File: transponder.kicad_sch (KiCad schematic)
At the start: 5 parts, among them J1 Antenna SMA, J2 DB15_Female, J3 Screw_Terminal_01x08, J4 Screw_Terminal_01x12

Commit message: Proof reading and snagging updates
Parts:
- TB6: renamed from J4; symbol Connector:Screw_Terminal_01x12 -> Connector:Screw_Terminal_01x10
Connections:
- net GND: no longer TB6.11 (Pin_11), TB6.12 (Pin_12)
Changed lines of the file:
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@@
   (title_block
     (title "Europa Transponder")
-    (date "2022-11-24")
-    (rev "4")
-    (comment 1 "Comment 1")
+    (date "2022-12-22")
+    (rev "5")
   )
   (junction (at 180.34 63.5) (diameter 0) (color 0 0 0 0)
-  )
-  (junction (at 180.34 83.82) (diameter 0) (color 0 0 0 0)
   )
   (junction (at 180.34 60.96) (diameter 0) (color 0 0 0 0)
@@
   (junction (at 180.34 78.74) (diameter 0) (color 0 0 0 0)
   )
-  (junction (at 180.34 58.42) (diameter 0) (color 0 0 0 0)
-  )
   (junction (at 180.34 81.28) (diameter 0) (color 0 0 0 0)
   )
-  (junction (at 120.65 58.42) (diameter 0) (color 0 0 0 0)
+  (junction (at 120.65 60.96) (diameter 0) (color 0 0 0 0)
   )
   (junction (at 180.34 76.2) (diameter 0) (color 0 0 0 0)
@@
     (stroke (width 0) (type default) (color 0 0 0 0))
   )
-  (wire (pts (xy 180.34 83.82) (xy 180.34 87.63))
+  (wire (pts (xy 180.34 81.28) (xy 180.34 87.63))
     (stroke (width 0) (type default) (color 0 0 0 0))
   )
   (wire (pts (xy 180.34 78.74) (xy 180.34 81.28))
-    (stroke (width 0) (type default) (color 0 0 0 0))
-  )
-  (wire (pts (xy 180.34 81.28) (xy 180.34 83.82))
     (stroke (width 0) (type default) (color 0 0 0 0))
   )
@@
     (stroke (width 0) (type default) (color 0 0 0 0))
   )
-  (wire (pts (xy 180.34 55.88) (xy 180.34 58.42))
-    (stroke (width 0) (type default) (color 0 0 0 0))
-  )
   (polyline (pts (xy 109.22 44.45) (xy 109.22 123.19))
     (stroke (width 0) (type default) (color 0 0 0 0))
@@
   )
   (wire (pts (xy 171.45 91.44) (xy 171.45 105.41))
+    (stroke (width 0) (type default) (color 0 0 0 0))
+  )
+  (wire (pts (xy 120.65 60.96) (xy 180.34 60.96))
     (stroke (width 0) (type default) (color 0 0 0 0))
   )
@@
   )
   (wire (pts (xy 171.45 105.41) (xy 177.8 105.41))
-    (stroke (width 0) (type default) (color 0 0 0 0))
-  )
-  (wire (pts (xy 120.65 58.42) (xy 180.34 58.42))
     (stroke (width 0) (type default) (color 0 0 0 0))
   )
@@
     (effects (font (size 1.27 1.27)) (justify left bottom))
   )
-  (symbol (lib_id "Connector:Screw_Terminal_01x12") (at 185.42 68.58 0) (unit 1)
+  (symbol (lib_id "Connector:Screw_Terminal_01x10") (at 185.42 68.58 0) (unit 1)
     (in_bom yes) (on_board yes) (fields_autoplaced)
-    (property "Reference" "J4" (id 0) (at 187.96 68.5799 0)
+    (property "Reference" "TB6" (id 0) (at 187.96 68.5799 0)
       (effects (font (size 1.27 1.27)) (justify left))
     )
@@
     (pin "1")
     (pin "10")
-    (pin "11")
-    (pin "12")
     (pin "2")
     (pin "3")

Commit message: Added Tag Blocks
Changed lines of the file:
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@@
   (junction (at 180.34 63.5) (diameter 0) (color 0 0 0 0)
+  )
+  (junction (at 165.1 60.96) (diameter 0) (color 0 0 0 0)
   )
   (junction (at 180.34 60.96) (diameter 0) (color 0 0 0 0)
@@
   (junction (at 180.34 66.04) (diameter 0) (color 0 0 0 0)
   )
+  (junction (at 166.37 91.44) (diameter 0) (color 0 0 0 0)
+  )
   (polyline (pts (xy 85.09 44.45) (xy 85.09 123.19))
     (stroke (width 0) (type default) (color 0 0 0 0))
@@
   )
   (wire (pts (xy 180.34 78.74) (xy 180.34 81.28))
+    (stroke (width 0) (type default) (color 0 0 0 0))
+  )
+  (wire (pts (xy 165.1 60.96) (xy 180.34 60.96))
+    (stroke (width 0) (type default) (color 0 0 0 0))
+  )
+  (wire (pts (xy 166.37 91.44) (xy 171.45 91.44))
     (stroke (width 0) (type default) (color 0 0 0 0))
   )
@@
     (stroke (width 0) (type default) (color 0 0 0 0))
   )
+  (wire (pts (xy 165.1 58.42) (xy 165.1 60.96))
+    (stroke (width 0) (type default) (color 0 0 0 0))
+  )
   (wire (pts (xy 171.45 91.44) (xy 171.45 105.41))
     (stroke (width 0) (type default) (color 0 0 0 0))
   )
-  (wire (pts (xy 120.65 60.96) (xy 180.34 60.96))
+  (wire (pts (xy 120.65 60.96) (xy 165.1 60.96))
     (stroke (width 0) (type default) (color 0 0 0 0))
   )
@@
     (stroke (width 0) (type default) (color 0 0 0 0))
   )
+  (wire (pts (xy 166.37 87.63) (xy 166.37 91.44))
+    (stroke (width 0) (type default) (color 0 0 0 0))
+  )
   (polyline (pts (xy 219.71 99.06) (xy 219.71 128.27))
     (stroke (width 0) (type default) (color 0 0 0 0))
@@
     (stroke (width 0) (type default) (color 0 0 0 0))
   )
-  (wire (pts (xy 120.65 91.44) (xy 171.45 91.44))
+  (wire (pts (xy 120.65 91.44) (xy 166.37 91.44))
     (stroke (width 0) (type default) (color 0 0 0 0))
   )
@@
     (effects (font (size 1.27 1.27)) (justify left bottom))
   )
-  (label "Ground" (at 123.19 58.42 0)
+  (label "Ground" (at 123.19 60.96 0)
     (effects (font (size 1.27 1.27)) (justify left bottom))
   )
@@
     (effects (font (size 1.27 1.27)) (justify left bottom))
   )
+  (hierarchical_label "0volt" (shape input) (at 165.1 58.42 0)
+    (effects (font (size 1.27 1.27)) (justify left))
+  )
+  (hierarchical_label "+12v" (shape input) (at 166.37 87.63 0)
+    (effects (font (size 1.27 1.27)) (justify left))
+  )
   (symbol (lib_id "Connector:Screw_Terminal_01x10") (at 185.42 68.58 0) (unit 1)

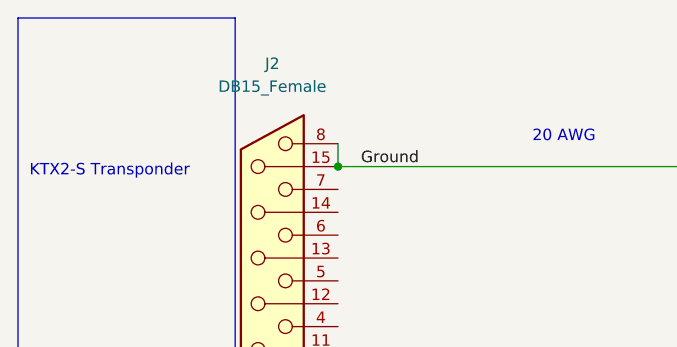
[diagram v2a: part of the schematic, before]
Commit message: Updates from manual validation
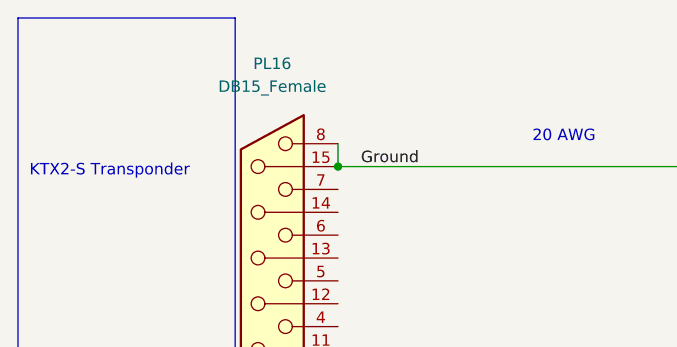
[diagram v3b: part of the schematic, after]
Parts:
- renumbered J2 to PL16
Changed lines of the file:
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@@
   (title_block
     (title "Europa Transponder")
-    (date "2022-12-22")
-    (rev "5")
+    (date "2022-12-24")
+    (rev "6")
   )
   (junction (at 180.34 63.5) (diameter 0) (color 0 0 0 0)
@@
   (symbol (lib_id "Connector:DB15_Female") (at 113.03 76.2 180) (unit 1)
     (in_bom yes) (on_board yes) (fields_autoplaced)
-    (property "Reference" "J2" (id 0) (at 113.3475 49.53 0))
+    (property "Reference" "PL16" (id 0) (at 113.3475 49.53 0))
     (property "Value" "DB15_Female" (id 1) (at 113.3475 52.07 0))
     (property "Footprint" "" (id 2) (at 113.03 76.2 0)

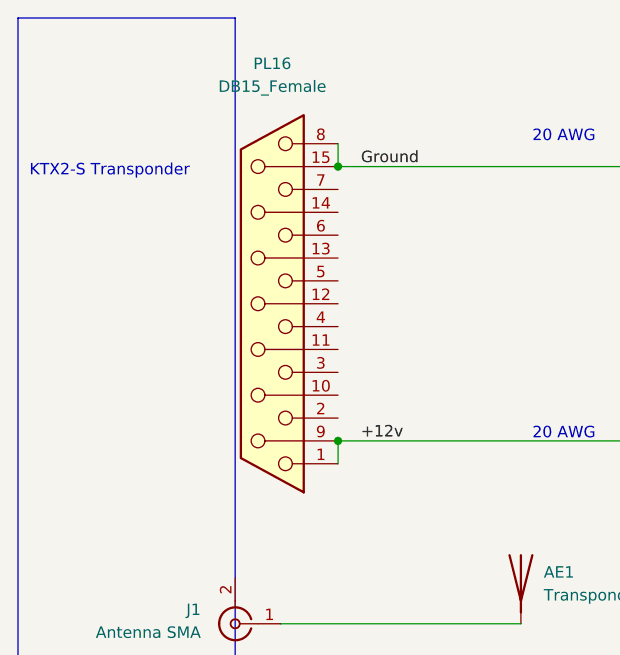
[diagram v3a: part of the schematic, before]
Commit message: Completed content of Connectors sheet, started SmartAss sheet
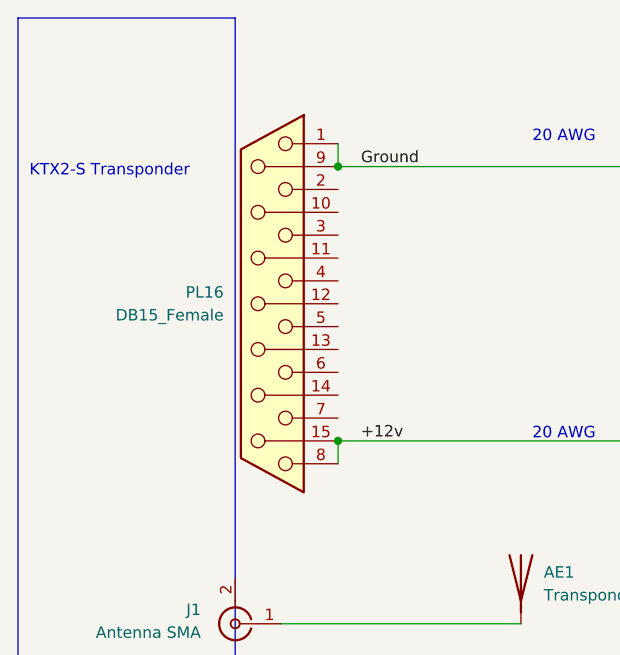
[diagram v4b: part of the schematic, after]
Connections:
- net +12v: now also PL16.15 (P15), PL16.8; no longer PL16.1, PL16.9 (P9)
- net GND: now also PL16.1, PL16.9 (P9); no longer PL16.15 (P15), PL16.8
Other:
- moved on the sheet: PL16
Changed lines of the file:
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@@
   (title_block
     (title "Europa Transponder")
-    (date "2022-12-24")
-    (rev "6")
+    (date "2022-12-27")
+    (rev "7")
   )
   (junction (at 180.34 63.5) (diameter 0) (color 0 0 0 0)
   )
+  (junction (at 120.65 60.96) (diameter 0) (color 0 0 0 0)
+  )
+  (junction (at 180.34 60.96) (diameter 0) (color 0 0 0 0)
+  )
+  (junction (at 180.34 68.58) (diameter 0) (color 0 0 0 0)
+  )
+  (junction (at 180.34 78.74) (diameter 0) (color 0 0 0 0)
+  )
   (junction (at 165.1 60.96) (diameter 0) (color 0 0 0 0)
   )
-  (junction (at 180.34 60.96) (diameter 0) (color 0 0 0 0)
-  )
-  (junction (at 180.34 68.58) (diameter 0) (color 0 0 0 0)
-  )
-  (junction (at 180.34 78.74) (diameter 0) (color 0 0 0 0)
-  )
   (junction (at 180.34 81.28) (diameter 0) (color 0 0 0 0)
   )
-  (junction (at 120.65 60.96) (diameter 0) (color 0 0 0 0)
-  )
   (junction (at 180.34 76.2) (diameter 0) (color 0 0 0 0)
   )
   (junction (at 180.34 73.66) (diameter 0) (color 0 0 0 0)
   )
+  (junction (at 180.34 71.12) (diameter 0) (color 0 0 0 0)
+  )
+  (junction (at 180.34 66.04) (diameter 0) (color 0 0 0 0)
+  )
   (junction (at 120.65 91.44) (diameter 0) (color 0 0 0 0)
   )
-  (junction (at 180.34 71.12) (diameter 0) (color 0 0 0 0)
-  )
-  (junction (at 180.34 66.04) (diameter 0) (color 0 0 0 0)
-  )
   (junction (at 166.37 91.44) (diameter 0) (color 0 0 0 0)
   )
@@
     (stroke (width 0) (type default) (color 0 0 0 0))
   )
+  (wire (pts (xy 120.65 60.96) (xy 165.1 60.96))
+    (stroke (width 0) (type default) (color 0 0 0 0))
+  )
   (wire (pts (xy 171.45 91.44) (xy 171.45 105.41))
-    (stroke (width 0) (type default) (color 0 0 0 0))
-  )
-  (wire (pts (xy 120.65 60.96) (xy 165.1 60.96))
     (stroke (width 0) (type default) (color 0 0 0 0))
   )
@@
     (pin "2")
   )
-  (symbol (lib_id "Connector:DB15_Female") (at 113.03 76.2 180) (unit 1)
-    (in_bom yes) (on_board yes) (fields_autoplaced)
-    (property "Reference" "PL16" (id 0) (at 113.3475 49.53 0))
-    (property "Value" "DB15_Female" (id 1) (at 113.3475 52.07 0))
+  (symbol (lib_id "Connector:DB15_Female") (at 113.03 76.2 0) (mirror y) (unit 1)
+    (in_bom yes) (on_board yes) (fields_autoplaced)
+    (property "Reference" "PL16" (id 0) (at 107.95 74.9299 0)
+      (effects (font (size 1.27 1.27)) (justify left))
+    )
+    (property "Value" "DB15_Female" (id 1) (at 107.95 77.4699 0)
+      (effects (font (size 1.27 1.27)) (justify left))
+    )
     (property "Footprint" "" (id 2) (at 113.03 76.2 0)
       (effects (font (size 1.27 1.27)) hide)
